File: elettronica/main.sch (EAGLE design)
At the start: 58 parts, among them IC1 74LS595D, IC2 7805T, J2 2X6, J3 455-1750-1-ND

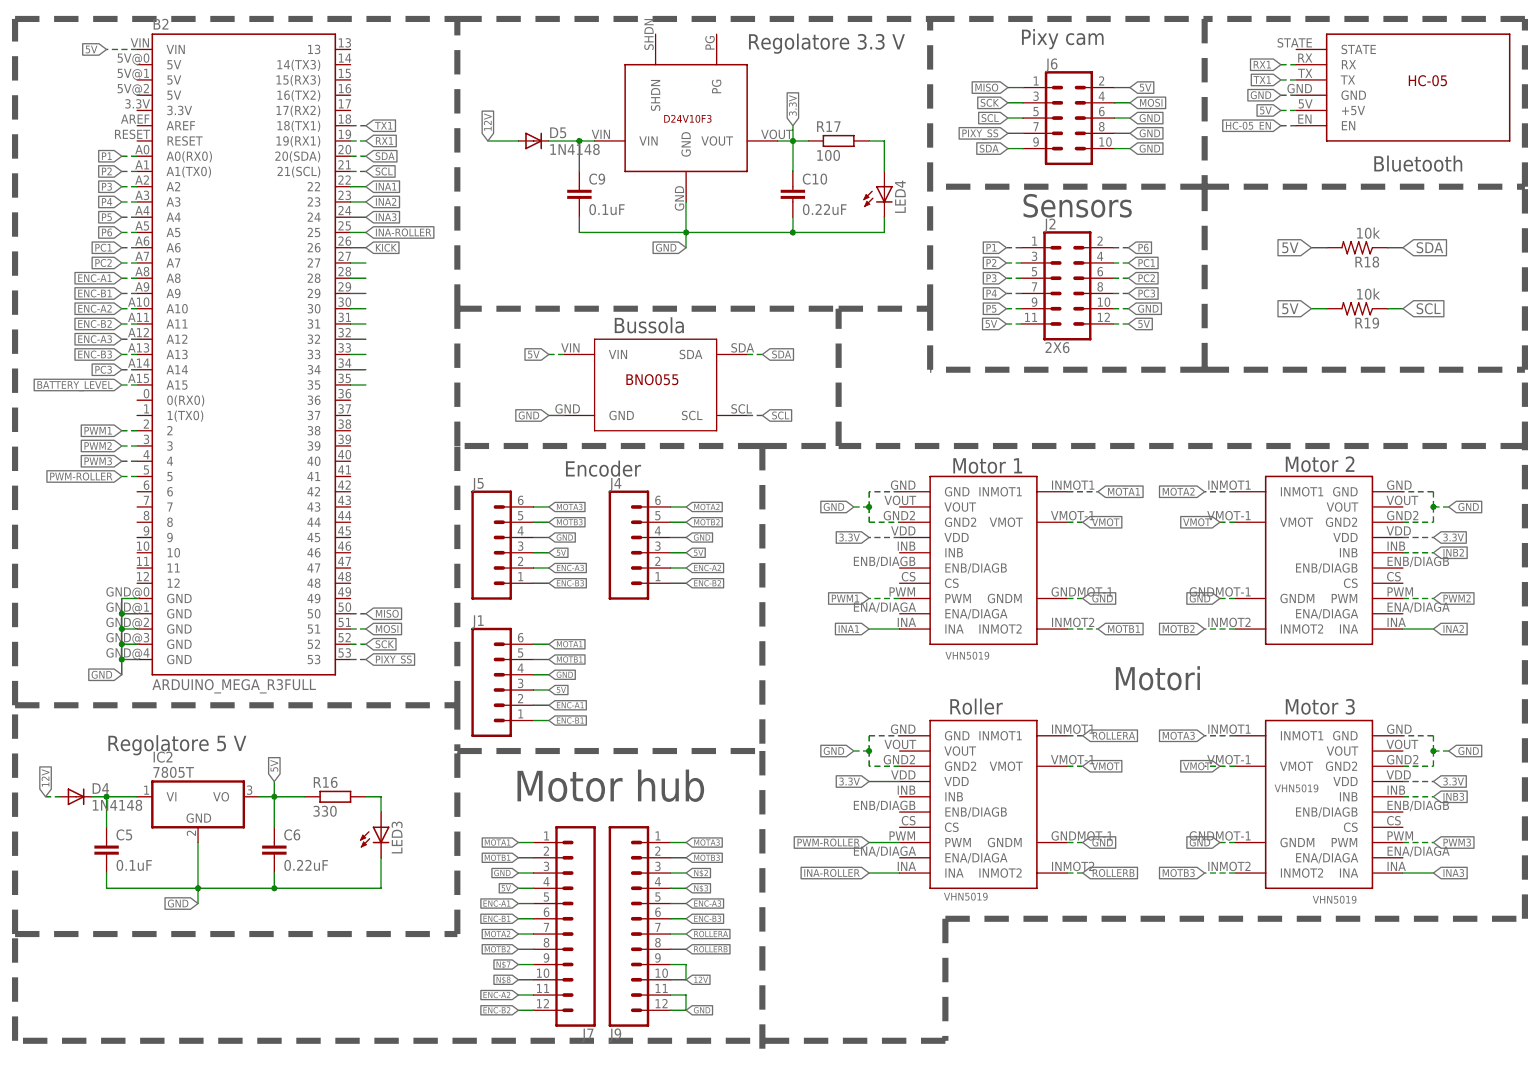
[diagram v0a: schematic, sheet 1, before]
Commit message: posizionare i pezzi nella board
aggiute anche ulp per autoposizionamento e drc sparkfun
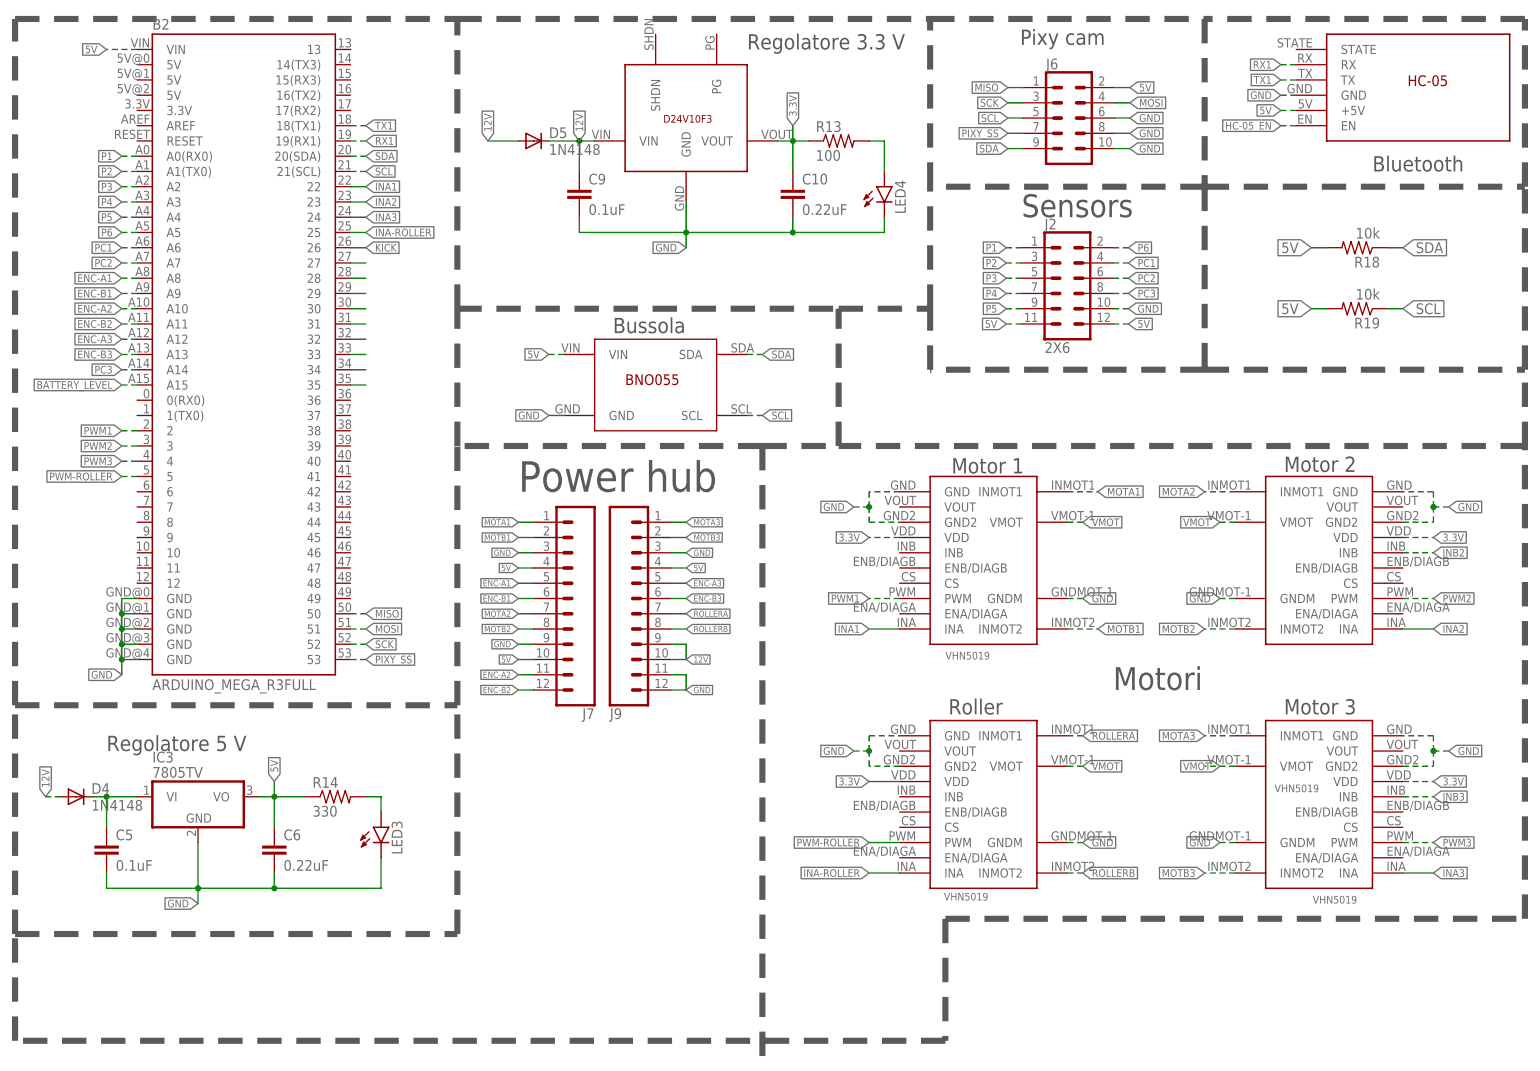
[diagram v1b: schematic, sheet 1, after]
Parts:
- removed D11, D12, D13, D14, D15, D16, D17: GREEN, SparkFun-LED:LED-GREEN1206
- removed IC2: 7805T, linear:7805T
- removed J1, J4, J5: (no value), SparkFun-Connectors:CONN_06SILK_FEMALE_PTH
- removed R16: 330, eagle-ltspice:R0204/7
- removed R17: 100, eagle-ltspice:R0204/7
- added D1, D10, D3, D6, D7, D8, D9: GREEN, SparkFun-LED:LED-GREEN1206
- added IC3: 7805TV, linear:7805TV
- added R13: 100, resistor:R-US_M1206
- added R14: 330, resistor:R-US_M1206
- LED3, LED4: value TLLR4400 -> GREEN; device led:TLLR4400 -> SparkFun-LED:LED-GREEN1206
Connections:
- removed net N$2: J9.3
- removed net N$3: J9.4
- removed net N$6: C9.1, D5.C, U$19.VIN
- removed net N$7: J7.9
- removed net N$8: J7.10
- net 12V: now also C9.1, D5.C, IC3.VI, U$19.VIN; no longer IC2.VI
- net 3.3V: now also R13.1; no longer R17.1
- net 5V: now also IC3.VO, J7.10, J9.4, R14.1; no longer IC2.VO, J1.3, J4.3, J5.3, R16.1
- net ENC-A1: no longer J1.2
- net ENC-A2: no longer J4.2
- net ENC-A3: no longer J5.2
- net ENC-B1: no longer J1.1
- net ENC-B2: no longer J4.1
- net ENC-B3: no longer J5.1
- net GND: now also IC3.GND, J7.9, J9.3; no longer IC2.GND, J1.4, J4.4, J5.4
- net LED1: now also D1.A, D1.C; no longer D11.A, D11.C
- net LED2: now also D3.A, D3.C; no longer D12.A, D12.C
- net LED3: now also D6.A, D6.C; no longer D13.A, D13.C
- net LED4: now also D7.A, D7.C; no longer D14.A, D14.C
- net LED5: now also D8.A, D8.C; no longer D15.A, D15.C
- net LED6: now also D9.A, D9.C; no longer D16.A, D16.C
- net LED7: now also D10.A, D10.C; no longer D17.A, D17.C
- net MOTA1: no longer J1.6
- net MOTA2: no longer J4.6
- net MOTA3: no longer J5.6
- net MOTB1: no longer J1.5
- net MOTB2: no longer J4.5
- net MOTB3: no longer J5.5
- net N$1: now also R14.2; no longer R16.2
- net N$21: now also R13.2; no longer R17.2
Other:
- note added: "Power hub"
- note removed: "Encoder"
- note removed: "Motor hub"
- moved on the sheet: J7, J9

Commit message: continuare a posizionare i pezzi nella board
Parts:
- removed D2: 1N4148, diode:1N4148DO35-7
- removed J3: 455-1750-1-ND, SparkFun-Connectors:CONN_03
- removed R1: 10k, eagle-ltspice:RR1206
- removed R2: 100, eagle-ltspice:RR1206
- removed U$17: BNO055, BNO055:BNO055
- removed X2: (no value), con-ptr500:AK500/2-H
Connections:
- removed net DRAIN: J3.2, X2-2.KL
- new net N$2: D1.C, R3.2
- new net N$3: D3.C, R4.2
- new net N$6: D8.C, R7.2
- new net N$7: D9.C, R8.2
- new net N$8: D10.C, R9.2
- net 12V: no longer X2-1.KL
- net 5V: no longer U$17.VIN
- net GND: no longer J3.3, R1.2, U$17.GND
- net KICK: no longer R2.2
- net LED1: no longer D1.C, R3.2
- net LED2: no longer D3.C, R4.2
- net LED3: no longer D6.C, R5.2
- net LED4: no longer D7.C, R6.2
- net LED5: no longer D8.C, R7.2
- net LED6: no longer D9.C, R8.2
- net LED7: no longer D10.C, R9.2
- net N$4: now also D6.C, R5.2; no longer D2.C, J3.1, R1.1
- net N$5: now also D7.C, R6.2; no longer D2.A, R2.1
- net SCL: no longer U$17.SCL
- net SDA: no longer U$17.SDA
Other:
- note added: "connesso a bus i2c"
- note removed: "Solenoid"
- note removed: "stp16nf06"

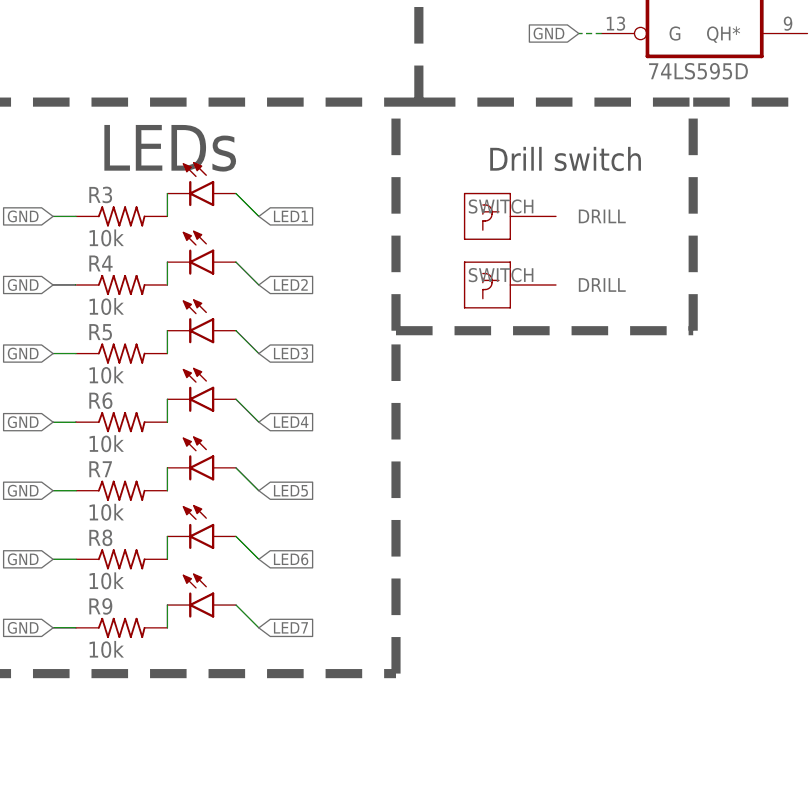
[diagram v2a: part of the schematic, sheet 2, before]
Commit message: PCB Finita
posizionati tutti i componenti e tracciate tutte le piste
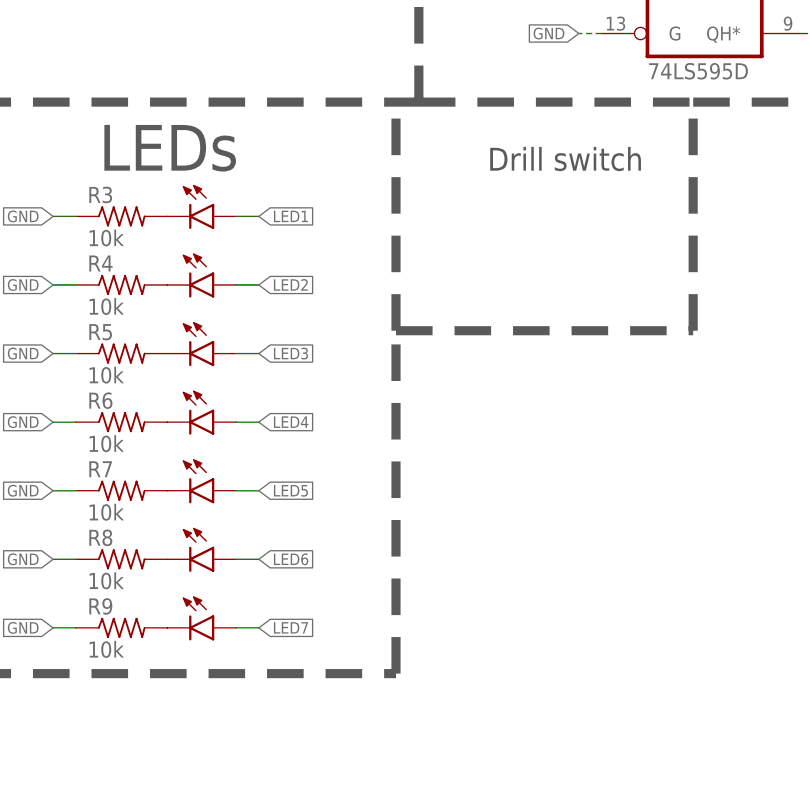
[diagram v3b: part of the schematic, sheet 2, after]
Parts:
- removed U$3, U$8: DRILL_SWITCH, Switch drill:DRILL_SWITCH
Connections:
- removed net N$22: B2.27
- removed net N$26: B2.28
- removed net N$27: B2.29
- removed net N$28: B2.30
- removed net N$29: B2.31
- removed net N$30: B2.32
- removed net N$31: B2.33
- removed net N$32: B2.34
- removed net N$33: B2.35
- new net 12VTO3.3: C9.1, D5.C, U$19.VIN
- new net 12VTO5: C5.1, D4.C, IC3.VI
- net 12V: no longer C5.1, C9.1, D4.C, D5.C, IC3.VI, U$19.VIN

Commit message: pcb definitiva 2.0
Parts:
- added J1: (no value), SparkFun-Connectors:CONN_03
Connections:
- net GND: now also J1.1
- net KICK: now also J1.3
- net VMOT: now also J1.2
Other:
- note added: "kicker"
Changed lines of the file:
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@@
 <part name="R13" library="resistor" library_urn="urn:adsk.eagle:library:348" deviceset="R-US_" device="M1206" package3d_urn="urn:adsk.eagle:package:26088/1" value="100"/>
 <part name="R14" library="resistor" library_urn="urn:adsk.eagle:library:348" deviceset="R-US_" device="M1206" package3d_urn="urn:adsk.eagle:package:26088/1" value="330"/>
+<part name="J1" library="SparkFun-Connectors" library_urn="urn:adsk.eagle:library:513" deviceset="CONN_03" device="" package3d_urn="urn:adsk.eagle:package:38063/1"/>
 </parts>
 <sheets>
@@
 </segment>
 </net>
-<net name="KICK" class="0">
+<net name="KICK" class="3">
 <segment>
 <pinref part="B2" gate="G$1" pin="26"/>
@@
 <wire x1="177.8" y1="134.62" x2="233.68" y2="134.62" width="1.016" layer="97" style="longdash"/>
 <wire x1="233.68" y1="134.62" x2="233.68" y2="175.26" width="1.016" layer="97" style="longdash"/>
+<text x="22.86" y="165.1" size="5.08" layer="97">kicker</text>
 </plain>
 <instances>
@@
 <instance part="D9" gate="G$1" x="38.1" y="83.82" smashed="yes" rot="R270"/>
 <instance part="D10" gate="G$1" x="38.1" y="76.2" smashed="yes" rot="R270"/>
+<instance part="J1" gate="J$1" x="17.78" y="152.4" smashed="yes">
+<attribute name="VALUE" x="15.24" y="145.034" size="1.778" layer="96" font="vector"/>
+<attribute name="NAME" x="15.24" y="157.988" size="1.778" layer="95" font="vector"/>
+</instance>
 </instances>
 <busses>
@@
 <label x="182.88" y="167.64" size="1.27" layer="95" xref="yes"/>
 </segment>
+<segment>
+<pinref part="J1" gate="J$1" pin="1"/>
+<wire x1="25.4" y1="149.86" x2="27.94" y2="149.86" width="0.1524" layer="91"/>
+<label x="27.94" y="149.86" size="1.27" layer="95" xref="yes"/>
+</segment>
 </net>
 <net name="3.3V" class="4">
@@
 <wire x1="162.56" y1="165.1" x2="165.1" y2="165.1" width="0.1524" layer="91"/>
 <label x="165.1" y="165.1" size="1.27" layer="95" xref="yes"/>
+</segment>
+<segment>
+<pinref part="J1" gate="J$1" pin="2"/>
+<wire x1="25.4" y1="152.4" x2="27.94" y2="152.4" width="0.1524" layer="91"/>
+<label x="27.94" y="152.4" size="1.27" layer="95" xref="yes"/>
 </segment>
 </net>
@@
 </segment>
 </net>
+<net name="KICK" class="3">
+<segment>
+<pinref part="J1" gate="J$1" pin="3"/>
+<wire x1="25.4" y1="154.94" x2="27.94" y2="154.94" width="0.1524" layer="91"/>
+<label x="27.94" y="154.94" size="1.27" layer="95" xref="yes"/>
+</segment>
+</net>
